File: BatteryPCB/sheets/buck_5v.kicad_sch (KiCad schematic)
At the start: 15 parts, among them U1 LMR51430XFDDCR

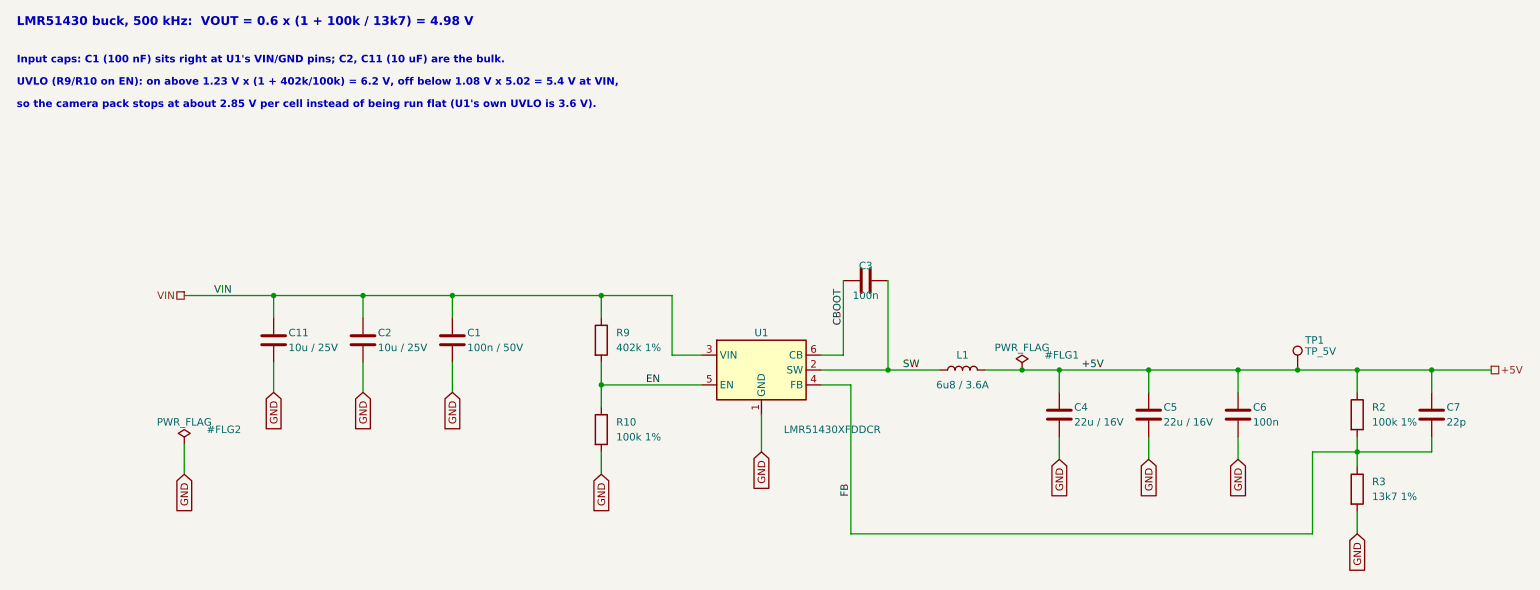
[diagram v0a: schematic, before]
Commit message: Battery PCB schematic: ESP32, camera and pack-sense sheets merged; C9/C10 on the buck output
Schematic only: sheets 3-5 become one wired sheet (3. ESP32 + camera), C9/C10 move
to the buck sheet's +5V output, supplies renumbered 6 -> 4. Every connection,
part, value and footprint is unchanged; the board only gets the new sheet paths
and net-name prefixes (tools/sync_from_sch.py). Gerbers and drills are
geometrically identical to v22. DRC 0 with schematic parity.

Co-Authored-By: Claude Opus 5.5 <noreply@anthropic.com>
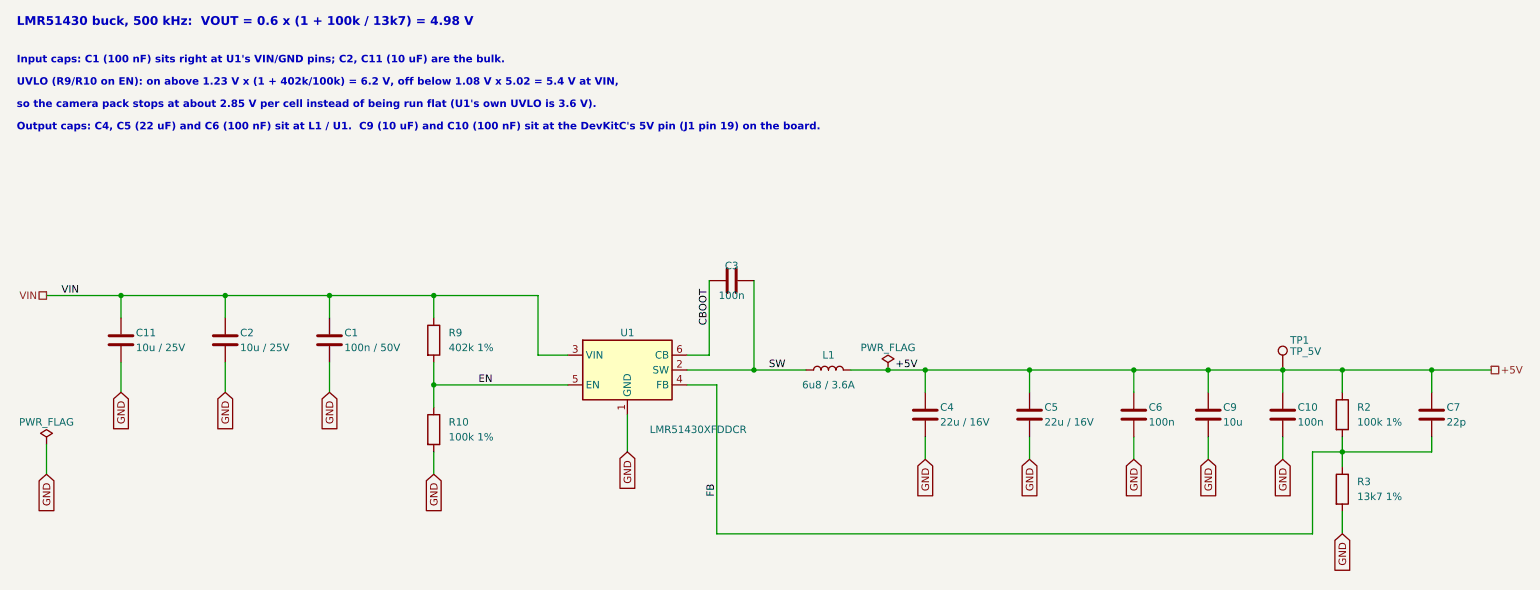
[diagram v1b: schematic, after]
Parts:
- added C10: 100n, Capacitor_SMD:C_0603_1608Metric, symbol Device:C
- added C9: 10u, Capacitor_SMD:C_0805_2012Metric, symbol Device:C
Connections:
- net +5V: now also C10.1, C9.1
- net GND: now also C10.2, C9.2
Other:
- note added: "Output caps: C4, C5 (22 uF) and C6 (100 nF) sit at L1 / U1. C9 (10 uF) and C10 (100 nF) sit at the DevKitC's 5V pin (J1 pin 19) on the board."
- moved on the sheet: C1, C11, C2, C3, C4, C5, C6, L1, R10, R2, R3, R9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

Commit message: Battery PCB v23: review 3 fixes (5 V setpoint, boot cap, GND vias, antenna keep-out)
- R3 13k7 -> 13k (RC0603FR-0713KL, LCSC C137796): 5.22 V nominal,
  5.05-5.39 V worst case, so the RunCam always gets >= 5.0 V.
- C3 moved beside U1; its SW side lands directly on L1's pad (no vias).
- New GND via ~1 mm from U1 pin 1; 5 stitching vias in open GND pour.
- Front antenna no-pour area now matches the back keep-out (48 x 21 mm).
- R10 pad 2 solid to the pour plus a trace to its via.
- fab/ regenerated (BOM, Gerbers, drills, schematic PDF, project zip).

ERC 0 errors; DRC 0 violations / 0 unconnected / 0 parity (also with
zones refilled); verify_A ALL PASS.

Co-Authored-By: Claude Opus 5.5 <noreply@anthropic.com>
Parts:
- R3: value 13k7 1% -> 13k 1%; MPN RC0603FR-0713K7L -> RC0603FR-0713KL
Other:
- note added: "LMR51430 buck, 500 kHz: VOUT = 0.6 x (1 + 100k / 13k) = 5.22 V"
- note removed: "LMR51430 buck, 500 kHz: VOUT = 0.6 x (1 + 100k / 13k7) = 4.98 V"
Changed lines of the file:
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@@
 		)
 	)
-	(text "LMR51430 buck, 500 kHz:  VOUT = 0.6 x (1 + 100k / 13k7) = 4.98 V"
+	(text "LMR51430 buck, 500 kHz:  VOUT = 0.6 x (1 + 100k / 13k) = 5.22 V"
 		(exclude_from_sim no)
 		(at 25.4 30.48 0)
@@
 			)
 		)
-		(property "Value" "13k7 1%"
+		(property "Value" "13k 1%"
 			(at 254 110.49 0)
 			(show_name no)
@@
 			)
 		)
-		(property "MPN" "RC0603FR-0713K7L"
+		(property "MPN" "RC0603FR-0713KL"
 			(at 251.46 109.22 0)
 			(hide yes)
